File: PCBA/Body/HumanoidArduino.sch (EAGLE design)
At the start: 88 parts, among them IC1 7805TV, J2 22-27-2041-04, Q1 12MHz, U4 CH340G, U5 SX1308_B628, X1 MINI-USB-UX60-MB-5S8

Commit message: PCBA again
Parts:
- removed F25, F26: POLYSWITCH, HumanoidLbr:POLYSWITCH
- removed JP26, JP27: JUMPER_3X1_0.1, HumanoidLbr:JUMPER_3X1_0.1
- removed R2: (no value), SparkFun-Resistors:RESISTOR-ARRAY0603-ARV
- added C5: 22u, capacitor-wima:C2,5-3
- added U6: MCP73213-A6SI/MF, DFN300X300X100-11N:MCP73213-A6SI/MF
- C4: value 22p -> 22u
- L1: value (none) -> 15uH
- R1: value (none) -> 10k; device SparkFun-Resistors:RESISTOR-ARRAY0603-ARV -> SparkFun-Passives:RESISTOR0805-RES
- R11: value 670R -> 18k
- R12: value 670R -> 1k
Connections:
- removed net N$51: F25.P$1, JP26.2
- removed net N$52: F26.P$1, JP27.2
- new net N$62: U6.VDD@2
- new net N$63: U6.VBAT@1
- new net N$64: R1.2, U6.PROG
- net +5V: no longer F25.P$2, F26.P$2
- net GND: now also C5.2, JP10.3, JP11.3, JP12.3, JP13.3, JP14.3, JP15.3, JP16.3, JP17.3, JP5.3, JP6.3, JP7.3, JP8.3, R1.1, U6.VSS@2; no longer JP26.3, JP27.3
- net N$59: now also R11.1
- net PWM12: no longer R3A.2
- net PWM13: no longer R3B.2
- net PWM14: no longer R3C.2
- net PWM15: no longer R3D.2
- net PWM22: now also R10B.1
- net PWM24: now also R3D.2
- net PWM25: now also R3C.2
- net PWM26: now also R3B.2
- net PWM27: now also R3A.2
- net V-CHG: now also C5.1
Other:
- note added: "12V Boost"
- note added: "5A Schottky"
- note added: "MOUNTING HOLES"
- note added: "USB LIPO CHARGER"
- note added: "USB UART COMMS"
- note added: "~11.4V"
- moved on the sheet: C1, C2, C3, C4, D1, F1, F10, F11, F12, F13, F14, F15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

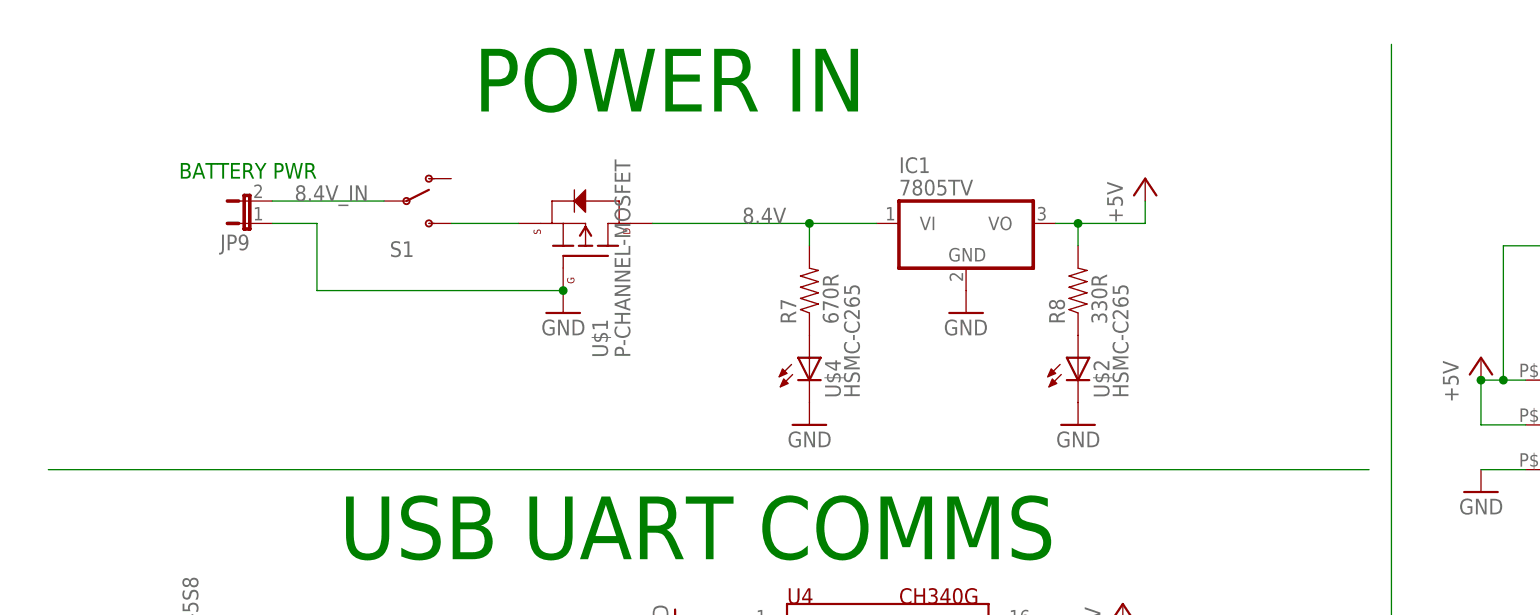
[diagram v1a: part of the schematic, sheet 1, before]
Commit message: Using proper 5V buck reg
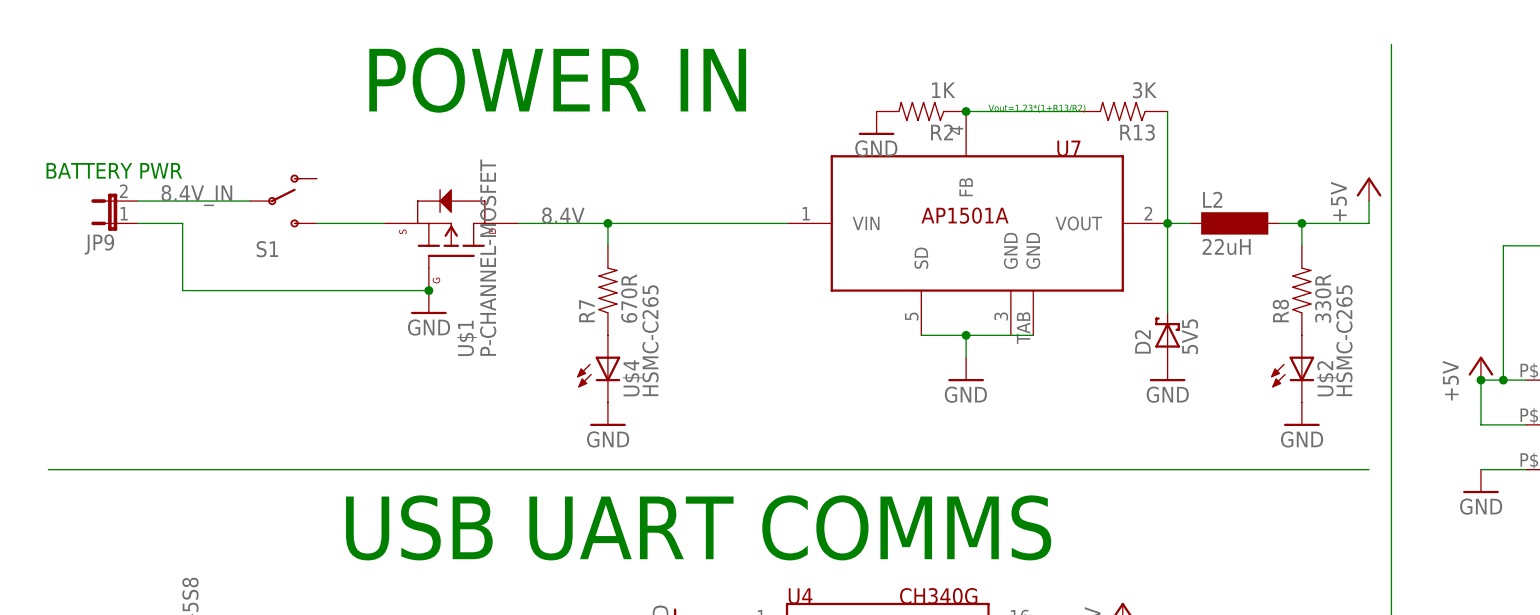
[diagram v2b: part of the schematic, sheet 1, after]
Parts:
- removed IC1: 7805TV, linear:7805TV
- added D2: 5V5, diode:BAT60J
- added L2: 22uH, inductor-neosid:MS85
- added R13: 3K, SparkFun-Passives:RESISTOR0805-RES
- added R2: 1K, SparkFun-Passives:RESISTOR0805-RES
- added U7: AP1501A, TO-263-5:AP1501A
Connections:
- new net N$65: R13.2, R2.1, U7.FB
- new net N$66: D2.C, L2.1, R13.1, U7.VOUT
- net +5V: now also L2.2; no longer IC1.VO
- net 8.4V: now also U7.VIN; no longer IC1.VI
- net GND: now also D2.A, R2.2, U7.GND@2, U7.SD; no longer IC1.GND
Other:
- note added: "Vout=1.23*(1+R13/R2)"
- moved on the sheet: JP9, R7, R8, S1, U$1, U$2, U$4
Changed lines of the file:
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@@
 <part name="H3" library="holes" deviceset="MOUNT-HOLE" device="3.6"/>
 <part name="U$3" library="ZMZE" deviceset="CHIP" device=""/>
-<part name="IC1" library="linear" deviceset="78*" device="TV" technology="05"/>
 <part name="GND2" library="supply1" deviceset="GND" device=""/>
 <part name="P+1" library="supply1" deviceset="+5V" device=""/>
@@
 <part name="GND29" library="supply1" deviceset="GND" device=""/>
 <part name="R1" library="SparkFun-Passives" deviceset="RESISTOR" device="0805-RES" value="10k"/>
+<part name="U7" library="TO-263-5" deviceset="AP1501A" device=""/>
+<part name="L2" library="inductor-neosid" deviceset="MS85" device="" value="22uH"/>
+<part name="D2" library="diode" deviceset="BAT60J" device="" value="5V5"/>
+<part name="GND30" library="supply1" deviceset="GND" device=""/>
+<part name="GND41" library="supply1" deviceset="GND" device=""/>
+<part name="R2" library="SparkFun-Passives" deviceset="RESISTOR" device="0805-RES" value="1K"/>
+<part name="R13" library="SparkFun-Passives" deviceset="RESISTOR" device="0805-RES" value="3K"/>
 </parts>
 <sheets>
@@
 <text x="353.06" y="220.98" size="1.778" layer="91" rot="MR0">BATTERY CHG</text>
 <text x="233.68" y="167.64" size="7.112" layer="91">SERVO PCA9685</text>
-<text x="55.88" y="246.38" size="7.112" layer="91">POWER IN</text>
+<text x="43.18" y="246.38" size="7.112" layer="91">POWER IN</text>
 <text x="50.8" y="149.86" size="7.112" layer="91">CONTROLLER</text>
 <text x="147.32" y="104.14" size="1.778" layer="91">*3V3 IO</text>
 <text x="261.62" y="162.56" size="1.778" layer="91">￼ ✓ 3V3 compliant</text>
 <text x="5.08" y="144.78" size="1.778" layer="91">5V@1A</text>
-<text x="38.1" y="238.76" size="1.778" layer="91" rot="MR0">BATTERY PWR</text>
+<text x="22.86" y="238.76" size="1.778" layer="91" rot="MR0">BATTERY PWR</text>
 <text x="182.88" y="15.24" size="7.112" layer="91">MOUNTING HOLES</text>
 <text x="40.64" y="195.58" size="7.112" layer="91">USB UART COMMS</text>
@@
 <text x="223.52" y="228.6" size="1.778" layer="91">~11.4V</text>
 <text x="198.12" y="226.06" size="1.778" layer="91">5A Schottky</text>
+<text x="114.3" y="246.38" size="0.762" layer="91">Vout=1.23*(1+R13/R2)</text>
 </plain>
 <instances>
@@
 <instance part="H3" gate="G$1" x="236.22" y="10.16"/>
 <instance part="U$3" gate="G$1" x="35.56" y="15.24"/>
-<instance part="IC1" gate="A1" x="111.76" y="233.68"/>
-<instance part="GND2" gate="1" x="111.76" y="223.52"/>
-<instance part="P+1" gate="1" x="132.08" y="238.76"/>
+<instance part="GND2" gate="1" x="111.76" y="215.9"/>
+<instance part="P+1" gate="1" x="157.48" y="238.76"/>
 <instance part="P+5" gate="1" x="20.32" y="144.78"/>
 <instance part="GND3" gate="1" x="353.06" y="215.9" rot="MR270"/>
@@
 <instance part="GND9" gate="1" x="304.8" y="124.46" rot="R90"/>
 <instance part="P+8" gate="1" x="312.42" y="157.48"/>
-<instance part="S1" gate="1" x="48.26" y="236.22"/>
-<instance part="U$1" gate="G$1" x="68.58" y="231.14" rot="R90"/>
-<instance part="GND14" gate="1" x="66.04" y="223.52" rot="MR0"/>
-<instance part="JP9" gate="A" x="30.48" y="233.68" rot="R90"/>
-<instance part="U$2" gate="G$1" x="124.46" y="218.44"/>
-<instance part="U$4" gate="G$1" x="93.98" y="218.44"/>
-<instance part="GND31" gate="1" x="93.98" y="210.82" rot="MR0"/>
-<instance part="GND32" gate="1" x="124.46" y="210.82" rot="MR0"/>
-<instance part="R7" gate="G$1" x="93.98" y="226.06" rot="R90"/>
-<instance part="R8" gate="G$1" x="124.46" y="226.06" rot="R90"/>
+<instance part="S1" gate="1" x="33.02" y="236.22"/>
+<instance part="U$1" gate="G$1" x="53.34" y="231.14" rot="R90"/>
+<instance part="GND14" gate="1" x="50.8" y="223.52" rot="MR0"/>
+<instance part="JP9" gate="A" x="15.24" y="233.68" rot="R90"/>
+<instance part="U$2" gate="G$1" x="149.86" y="218.44"/>
+<instance part="U$4" gate="G$1" x="71.12" y="218.44"/>
+<instance part="GND31" gate="1" x="71.12" y="210.82" rot="MR0"/>
+<instance part="GND32" gate="1" x="149.86" y="210.82" rot="MR0"/>
+<instance part="R7" gate="G$1" x="71.12" y="226.06" rot="R90"/>
+<instance part="R8" gate="G$1" x="149.86" y="226.06" rot="R90"/>
 <instance part="F1" gate="G$1" x="302.26" y="149.86"/>
 <instance part="F2" gate="G$1" x="302.26" y="139.7"/>
@@
 <instance part="GND29" gate="1" x="302.26" y="198.12" rot="MR0"/>
 <instance part="R1" gate="G$1" x="302.26" y="205.74" rot="R90"/>
+<instance part="U7" gate="G$1" x="111.76" y="233.68"/>
+<instance part="L2" gate="G$1" x="142.24" y="233.68"/>
+<instance part="D2" gate="G$1" x="134.62" y="220.98" rot="R90"/>
+<instance part="GND30" gate="1" x="134.62" y="215.9" rot="MR0"/>
+<instance part="GND41" gate="1" x="101.6" y="243.84"/>
+<instance part="R2" gate="G$1" x="106.68" y="246.38" rot="R180"/>
+<instance part="R13" gate="G$1" x="129.54" y="246.38" rot="R180"/>
 </instances>
 <busses>
@@
 <nets>
 <net name="GND" class="0">
-<segment>
-<pinref part="IC1" gate="A1" pin="GND"/>
-<pinref part="GND2" gate="1" pin="GND"/>
-</segment>
 <segment>
 <pinref part="J2" gate="-1" pin="S"/>
@@
 <pinref part="GND14" gate="1" pin="GND"/>
 <pinref part="JP9" gate="A" pin="1"/>
-<wire x1="33.02" y1="233.68" x2="38.1" y2="233.68" width="0.1524" layer="91"/>
-<wire x1="38.1" y1="233.68" x2="38.1" y2="226.06" width="0.1524" layer="91"/>
-<wire x1="38.1" y1="226.06" x2="66.04" y2="226.06" width="0.1524" layer="91"/>
-<junction x="66.04" y="226.06"/>
+<wire x1="17.78" y1="233.68" x2="22.86" y2="233.68" width="0.1524" layer="91"/>
+<wire x1="22.86" y1="233.68" x2="22.86" y2="226.06" width="0.1524" layer="91"/>
+<wire x1="22.86" y1="226.06" x2="50.8" y2="226.06" width="0.1524" layer="91"/>
+<junction x="50.8" y="226.06"/>
 </segment>
 <segment>
@@
 <junction x="302.26" y="200.66"/>
 </segment>
+<segment>
+<pinref part="D2" gate="G$1" pin="A"/>
+<pinref part="GND30" gate="1" pin="GND"/>
+</segment>
+<segment>
+<pinref part="GND41" gate="1" pin="GND"/>
+<pinref part="R2" gate="G$1" pin="2"/>
+</segment>
+<segment>
+<pinref part="U7" gate="G$1" pin="GND@2"/>
+<pinref part="GND2" gate="1" pin="GND"/>
+<wire x1="119.38" y1="220.98" x2="111.76" y2="220.98" width="0.1524" layer="91"/>
+<wire x1="111.76" y1="220.98" x2="111.76" y2="218.44" width="0.1524" layer="91"/>
+<pinref part="U7" gate="G$1" pin="SD"/>
+<wire x1="106.68" y1="220.98" x2="111.76" y2="220.98" width="0.1524" layer="91"/>
+<junction x="111.76" y="220.98"/>
+</segment>
 </net>
 <net name="\O\E" class="0">
@@
 <net name="8.4V" class="0">
 <segment>
-<pinref part="IC1" gate="A1" pin="VI"/>
-<label x="86.36" y="233.68" size="1.778" layer="95"/>
+<label x="63.5" y="233.68" size="1.778" layer="95"/>
 <pinref part="U$1" gate="G$1" pin="D"/>
-<wire x1="76.2" y1="233.68" x2="93.98" y2="233.68" width="0.1524" layer="91"/>
+<wire x1="60.96" y1="233.68" x2="71.12" y2="233.68" width="0.1524" layer="91"/>
 <pinref part="R7" gate="G$1" pin="2"/>
-<wire x1="93.98" y1="233.68" x2="101.6" y2="233.68" width="0.1524" layer="91"/>
-<wire x1="93.98" y1="231.14" x2="93.98" y2="233.68" width="0.1524" layer="91"/>
-<junction x="93.98" y="233.68"/>
+<wire x1="71.12" y1="233.68" x2="91.44" y2="233.68" width="0.1524" layer="91"/>
+<wire x1="71.12" y1="231.14" x2="71.12" y2="233.68" width="0.1524" layer="91"/>
+<junction x="71.12" y="233.68"/>
+<pinref part="U7" gate="G$1" pin="VIN"/>
 </segment>
 </net>
 <net name="+5V" class="0">
 <segment>
-<pinref part="IC1" gate="A1" pin="VO"/>
-<wire x1="121.92" y1="233.68" x2="124.46" y2="233.68" width="0.1524" layer="91"/>
 <pinref part="P+1" gate="1" pin="+5V"/>
-<wire x1="124.46" y1="233.68" x2="132.08" y2="233.68" width="0.1524" layer="91"/>
-<wire x1="132.08" y1="233.68" x2="132.08" y2="236.22" width="0.1524" layer="91"/>
+<wire x1="149.86" y1="233.68" x2="157.48" y2="233.68" width="0.1524" layer="91"/>
+<wire x1="157.48" y1="233.68" x2="157.48" y2="236.22" width="0.1524" layer="91"/>
 <pinref part="R8" gate="G$1" pin="2"/>
-<wire x1="124.46" y1="231.14" x2="124.46" y2="233.68" width="0.1524" layer="91"/>
-<junction x="124.46" y="233.68"/>
+<wire x1="149.86" y1="231.14" x2="149.86" y2="233.68" width="0.1524" layer="91"/>
+<pinref part="L2" gate="G$1" pin="2"/>
+<wire x1="147.32" y1="233.68" x2="149.86" y2="233.68" width="0.1524" layer="91"/>
+<junction x="149.86" y="233.68"/>
 </segment>
 <segment>
@@
 <pinref part="S1" gate="1" pin="S"/>
 <pinref part="U$1" gate="G$1" pin="S"/>
-<wire x1="53.34" y1="233.68" x2="60.96" y2="233.68" width="0.1524" layer="91"/>
+<wire x1="38.1" y1="233.68" x2="45.72" y2="233.68" width="0.1524" layer="91"/>
 </segment>
 </net>
@@
 <segment>
 <pinref part="S1" gate="1" pin="P"/>
-<wire x1="45.72" y1="236.22" x2="33.02" y2="236.22" width="0.1524" layer="91"/>
-<label x="35.56" y="236.22" size="1.778" layer="95"/>
+<wire x1="30.48" y1="236.22" x2="17.78" y2="236.22" width="0.1524" layer="91"/>
+<label x="20.32" y="236.22" size="1.778" layer="95"/>
 <pinref part="JP9" gate="A" pin="2"/>
 </segment>
@@
 </segment>
 </net>
+<net name="N$65" class="0">
+<segment>
+<pinref part="U7" gate="G$1" pin="FB"/>
+<pinref part="R2" gate="G$1" pin="1"/>
+<pinref part="R13" gate="G$1" pin="2"/>
+<wire x1="111.76" y1="246.38" x2="124.46" y2="246.38" width="0.1524" layer="91"/>
+<junction x="111.76" y="246.38"/>
+</segment>
+</net>
+<net name="N$66" class="0">
+<segment>
+<pinref part="R13" gate="G$1" pin="1"/>
+<pinref part="U7" gate="G$1" pin="VOUT"/>
+<wire x1="134.62" y1="246.38" x2="134.62" y2="233.68" width="0.1524" layer="91"/>
+<pinref part="L2" gate="G$1" pin="1"/>
+<wire x1="137.16" y1="233.68" x2="134.62" y2="233.68" width="0.1524" layer="91"/>
+<junction x="134.62" y="233.68"/>
+<pinref part="D2" gate="G$1" pin="C"/>
+<wire x1="134.62" y1="233.68" x2="134.62" y2="223.52" width="0.1524" layer="91"/>
+</segment>
+</net>

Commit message: selected a few more parts for the PCB
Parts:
- removed U3: (no value), adafruit:PCA9685
- L1: value 15uH -> 22uH; device inductor-neosid:SM-1206 -> inductor-neosid:MS85
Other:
- note added: "0805"
- note added: "Nom 15uH"
- note added: "Pin1/Case"
- note added: "Pin3"
- note added: "SB10100"
- note added: "TO-220"
- note removed: "HEAD PCBA"
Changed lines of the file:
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@@
 <part name="U1" library="adafruit" deviceset="PCA9685" device=""/>
 <part name="U2" library="adafruit" deviceset="PCA9685" device=""/>
-<part name="FRAME2" library="frames" deviceset="A3L-LOC" device=""/>
-<part name="U3" library="adafruit" deviceset="PCA9685" device=""/>
 <part name="GND1" library="supply1" deviceset="GND" device=""/>
 <part name="P+2" library="supply1" deviceset="+5V" device=""/>
@@
 <part name="C4" library="capacitor-wima" deviceset="C" device="2,5-3" value="22u"/>
 <part name="D1" library="avago" deviceset="HSMS-285B" device=""/>
-<part name="L1" library="inductor-neosid" deviceset="SM-1206" device="" value="15uH"/>
 <part name="P+12" library="supply1" deviceset="+5V" device=""/>
 <part name="C5" library="capacitor-wima" deviceset="C" device="2,5-3" value="22u"/>
@@
 <part name="R2" library="SparkFun-Passives" deviceset="RESISTOR" device="0805-RES" value="1K"/>
 <part name="R13" library="SparkFun-Passives" deviceset="RESISTOR" device="0805-RES" value="3K"/>
+<part name="L1" library="inductor-neosid" deviceset="MS85" device="" value="22uH"/>
 </parts>
 <sheets>
@@
 <text x="198.12" y="226.06" size="1.778" layer="91">5A Schottky</text>
 <text x="114.3" y="246.38" size="0.762" layer="91">Vout=1.23*(1+R13/R2)</text>
+<text x="68.58" y="177.8" size="0.762" layer="91">0805</text>
+<text x="185.42" y="233.68" size="0.762" layer="91">Nom 15uH</text>
+<text x="195.58" y="233.68" size="0.762" layer="91">SB10100</text>
+<text x="195.58" y="236.22" size="0.762" layer="91">TO-220</text>
+<text x="193.04" y="231.14" size="0.762" layer="91">Pin3</text>
+<text x="205.74" y="231.14" size="0.762" layer="91">Pin1/Case</text>
 </plain>
 <instances>
@@
 <instance part="C4" gate="G$1" x="218.44" y="200.66"/>
 <instance part="D1" gate="A" x="198.12" y="231.14"/>
-<instance part="L1" gate="G$1" x="185.42" y="231.14"/>
 <instance part="P+12" gate="1" x="370.84" y="157.48"/>
 <instance part="C5" gate="G$1" x="231.14" y="200.66"/>
@@
 <instance part="R2" gate="G$1" x="106.68" y="246.38" rot="R180"/>
 <instance part="R13" gate="G$1" x="129.54" y="246.38" rot="R180"/>
+<instance part="L1" gate="G$1" x="185.42" y="231.14"/>
 </instances>
 <busses>
@@
 <pinref part="U5" gate="G$1" pin="EN"/>
 <wire x1="170.18" y1="210.82" x2="175.26" y2="210.82" width="0.1524" layer="91"/>
-<pinref part="L1" gate="G$1" pin="1"/>
 <wire x1="172.72" y1="215.9" x2="172.72" y2="231.14" width="0.1524" layer="91"/>
 <wire x1="172.72" y1="231.14" x2="180.34" y2="231.14" width="0.1524" layer="91"/>
@@
 <pinref part="P+11" gate="1" pin="+5V"/>
 <junction x="170.18" y="215.9"/>
+<pinref part="L1" gate="G$1" pin="1"/>
 </segment>
 </net>
@@
 <wire x1="208.28" y1="215.9" x2="208.28" y2="226.06" width="0.1524" layer="91"/>
 <wire x1="208.28" y1="226.06" x2="193.04" y2="226.06" width="0.1524" layer="91"/>
-<pinref part="L1" gate="G$1" pin="2"/>
 <pinref part="D1" gate="A" pin="A"/>
 <wire x1="190.5" y1="231.14" x2="193.04" y2="231.14" width="0.1524" layer="91"/>
@@
 <wire x1="193.04" y1="226.06" x2="193.04" y2="231.14" width="0.1524" layer="91"/>
 <junction x="193.04" y="231.14"/>
+<pinref part="L1" gate="G$1" pin="2"/>
 </segment>
 </net>
@@
 <sheet>
 <plain>
-<text x="33.02" y="243.84" size="8.89" layer="91">HEAD PCBA</text>
 </plain>
 <instances>
-<instance part="FRAME2" gate="G$1" x="0" y="0"/>
-<instance part="U3" gate="G$1" x="91.44" y="177.8"/>
 </instances>
 <busses>

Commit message: working on PCBA
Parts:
- added LED1: (no value), led:LEDSML1206
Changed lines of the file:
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@@
 <part name="R13" library="SparkFun-Passives" deviceset="RESISTOR" device="0805-RES" value="3K"/>
 <part name="L1" library="inductor-neosid" deviceset="MS85" device="" value="22uH"/>
+<part name="LED1" library="led" deviceset="LED" device="SML1206"/>
 </parts>
 <sheets>
@@
 <instance part="R13" gate="G$1" x="129.54" y="246.38" rot="R180"/>
 <instance part="L1" gate="G$1" x="185.42" y="231.14"/>
+<instance part="LED1" gate="G$1" x="132.08" y="223.52"/>
 </instances>
 <busses>
